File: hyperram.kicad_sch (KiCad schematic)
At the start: 7 parts, among them U1 S27KL0641DABHI023

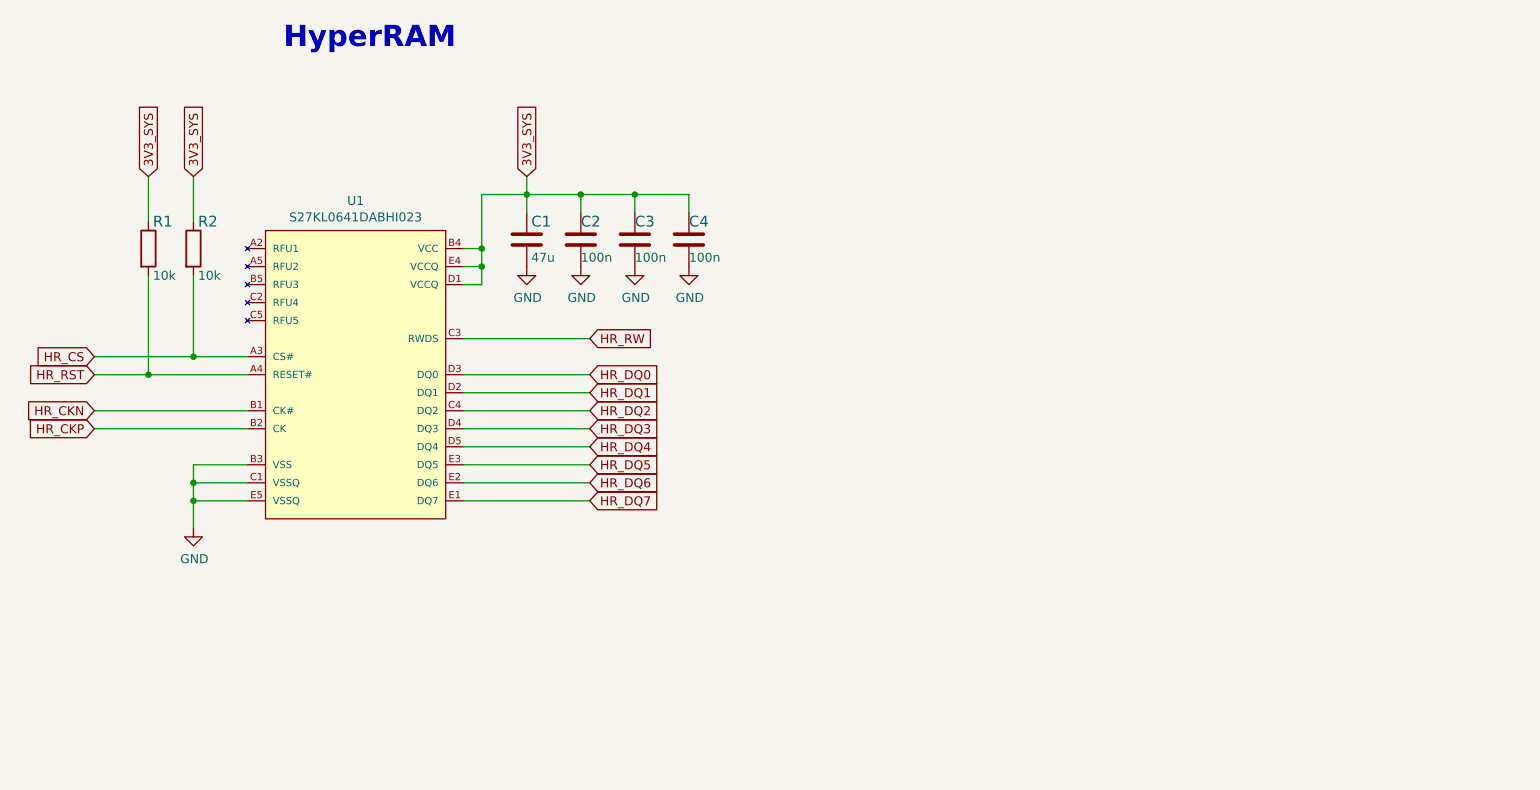
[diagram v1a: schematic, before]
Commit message: Introduce standardized components
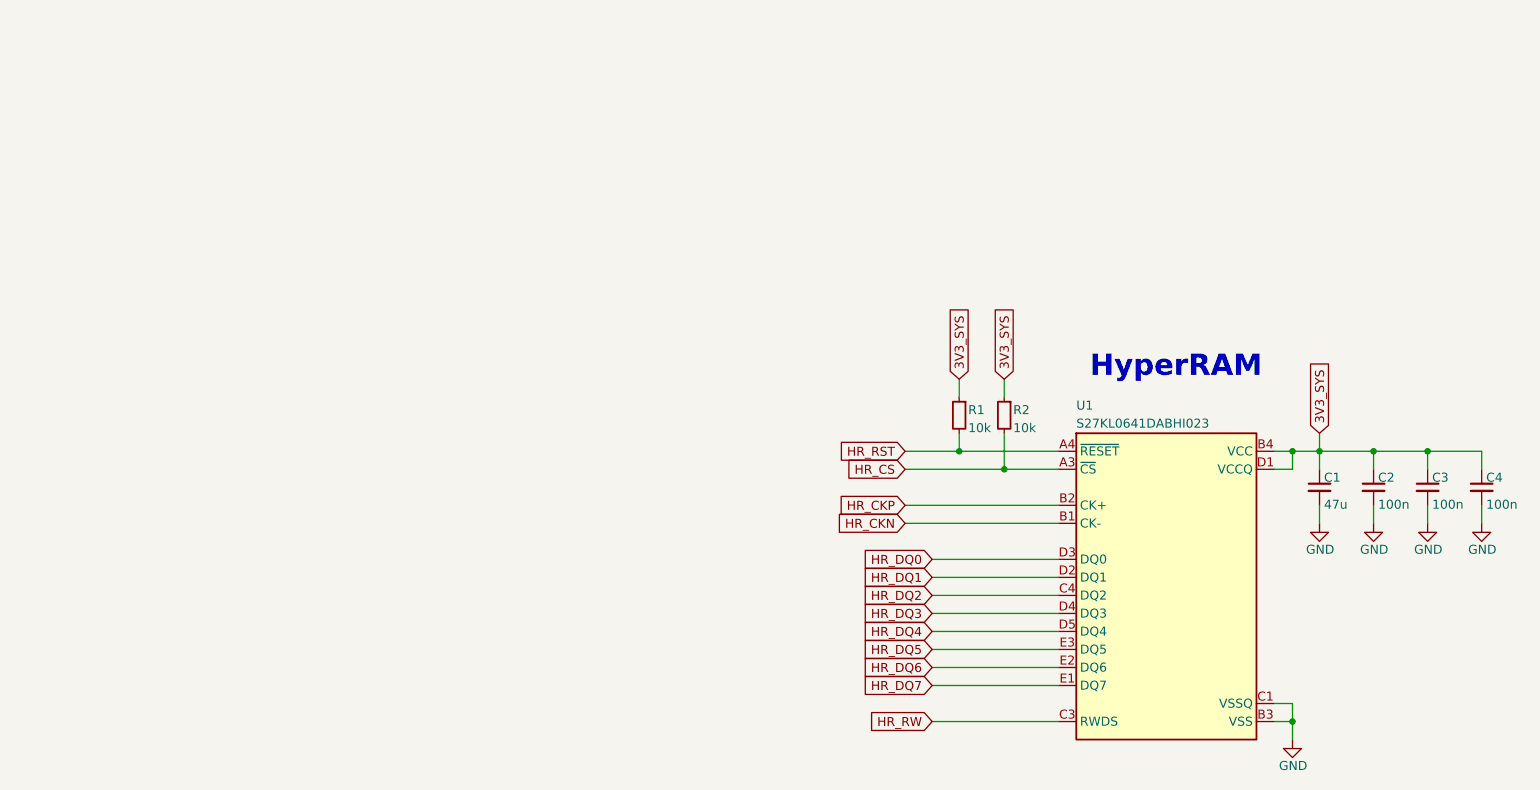
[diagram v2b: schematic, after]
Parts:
- C1: footprint lpddr4-test-board-footprints:0603-cap -> lpddr4-test-board-footprints:C_0603_1608Metric; Author (none) -> Antmicro; License (none) -> Apache-2.0; Manufacturer MURATA -> Murata
- C2, C3, C4: value C_100n_0402_6V3 -> C_100n_6V3_0402; footprint lpddr4-test-board-footprints:0402-cap -> lpddr4-test-board-footprints:C_0402_1005Metric; symbol lpddr4-test-board:C_100n_0402_6V3 -> lpddr4-test-board:C_100n_6V3_0402; Author (none) -> Antmicro; License (none) -> Apache-2.0
- R1, R2: footprint lpddr4-test-board-footprints:0402-res -> lpddr4-test-board-footprints:R_0402_1005Metric; Author (none) -> Antmicro; License (none) -> Apache-2.0; MPN CRCW040210K0FKEDHP -> CR0402-FX-1002GLF; Manufacturer VISHAY -> Bourns; Tolerance (none) -> 1%
- U1: footprint lpddr4-test-board-footprints:FBGA-24 -> lpddr4-test-board-footprints:FBGA-24-1_6x8mm_Layout5x5_P1mm; Author (none) -> Antmicro; License (none) -> Apache-2.0; Manufacturer CYPRESS SEMICONDUCTOR -> Cypress Semiconductor
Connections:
- net at U1.A2 (NC): now also U1.A5 (NC), U1.B5 (NC), U1.C2 (NC), U1.C5 (NC)
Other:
- moved on the sheet: C1, C2, C3, C4, R1, R2

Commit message: [#55158] components update
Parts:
- U1: footprint lpddr4-test-board-footprints:FBGA-24-1_6x8mm_Layout5x5_P1mm -> antmicro-footprints:FBGA-25-24_6x8mm_Layout5x5_P1mm
